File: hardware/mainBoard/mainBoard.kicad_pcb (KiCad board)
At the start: 2 copper layers, 99.9 x 52.5 mm, 24 parts, among them J1 UARTDebug, J2 LeftKeyConnector, J3 DisplayConnector, J4 RightKeyConnector, J5 EncoderConnector, U1 MCP4728-E_UN

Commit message: update wiring
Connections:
- A1 pad 16: Net-(A1-GPIO12) -> unconnected-(A1-GPIO12-Pad16)_1
- A1 pad 17: /LDAC -> unconnected-(A1-GPIO13-Pad17)
- A1 pad 19: unconnected-(A1-GPIO14-Pad19)_1 -> Net-(A1-GPIO14)
- A1 pad 20: unconnected-(A1-GPIO15-Pad20) -> /LDAC
- J3 pad 7: Net-(A1-GPIO12) -> Net-(A1-GPIO14)
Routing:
- net Net-(A1-GPIO12): track 20.3 -> 0.00 mm
- net Net-(A1-GPIO14): track 0.00 -> 13.8 mm
- net (no net): track 0.00 -> 0.80 mm
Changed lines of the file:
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@@
 			(layers "F.Cu" "F.Mask")
 			(roundrect_rratio 0.5)
-			(net "Net-(A1-GPIO12)")
+			(net "unconnected-(A1-GPIO12-Pad16)")
 			(pinfunction "GPIO12_16")
-			(pintype "bidirectional")
+			(pintype "bidirectional+no_connect")
 		)
 		(pad "16" thru_hole circle
@@
 			(layers "*.Cu" "*.Mask")
 			(remove_unused_layers no)
-			(net "Net-(A1-GPIO12)")
+			(net "unconnected-(A1-GPIO12-Pad16)_1")
 			(pinfunction "GPIO12_16")
-			(pintype "bidirectional")
+			(pintype "bidirectional+no_connect")
 		)
 		(pad "17" smd roundrect
@@
 			(layers "F.Cu" "F.Mask")
 			(roundrect_rratio 0.5)
-			(net "/LDAC")
+			(net "unconnected-(A1-GPIO13-Pad17)_1")
 			(pinfunction "GPIO13_17")
-			(pintype "bidirectional")
+			(pintype "bidirectional+no_connect")
 		)
 		(pad "17" thru_hole circle
@@
 			(layers "*.Cu" "*.Mask")
 			(remove_unused_layers no)
-			(net "/LDAC")
+			(net "unconnected-(A1-GPIO13-Pad17)")
 			(pinfunction "GPIO13_17")
-			(pintype "bidirectional")
+			(pintype "bidirectional+no_connect")
 		)
 		(pad "18" smd custom
@@
 			(layers "F.Cu" "F.Mask")
 			(roundrect_rratio 0.5)
-			(net "unconnected-(A1-GPIO14-Pad19)")
+			(net "Net-(A1-GPIO14)")
 			(pinfunction "GPIO14_19")
-			(pintype "bidirectional+no_connect")
+			(pintype "bidirectional")
 		)
 		(pad "19" thru_hole circle
@@
 			(layers "*.Cu" "*.Mask")
 			(remove_unused_layers no)
-			(net "unconnected-(A1-GPIO14-Pad19)_1")
+			(net "Net-(A1-GPIO14)")
 			(pinfunction "GPIO14_19")
-			(pintype "bidirectional+no_connect")
+			(pintype "bidirectional")
 		)
 		(pad "20" smd roundrect
@@
 			(layers "F.Cu" "F.Mask")
 			(roundrect_rratio 0.5)
-			(net "unconnected-(A1-GPIO15-Pad20)_1")
+			(net "/LDAC")
 			(pinfunction "GPIO15_20")
-			(pintype "bidirectional+no_connect")
+			(pintype "bidirectional")
 		)
 		(pad "20" thru_hole circle
@@
 			(layers "*.Cu" "*.Mask")
 			(remove_unused_layers no)
-			(net "unconnected-(A1-GPIO15-Pad20)")
+			(net "/LDAC")
 			(pinfunction "GPIO15_20")
-			(pintype "bidirectional+no_connect")
+			(pintype "bidirectional")
 		)
 		(pad "21" thru_hole circle
@@
 	)
 	(footprint "Connector_PinHeader_2.54mm:PinHeader_1x08_P2.54mm_Vertical"
+		(locked yes)
 		(layer "F.Cu")
 		(at 167.62 75.4 -90)
@@
 			(layers "*.Cu" "*.Mask")
 			(remove_unused_layers no)
-			(net "Net-(A1-GPIO12)")
+			(net "Net-(A1-GPIO14)")
 			(pinfunction "Pin_7_7")
 			(pintype "passive")
@@
 	)
 	(gr_text "CS"
+		(locked yes)
 		(at 163.110625 78.995238 90)
 		(layer "F.SilkS")
@@
 		)
 	)
-	(gr_text "GND"
-		(at 165.650625 80.090476 90)
+	(gr_text "VCC"
+		(at 165.650625 79.9 90)
 		(layer "F.SilkS")
 		(effects
@@
 		)
 	)
-	(gr_text "VCC"
-		(at 168.190625 79.9 90)
+	(gr_text "GND"
+		(at 168.190625 80.090476 90)
 		(layer "F.SilkS")
 		(effects
@@
 	)
 	(segment
+		(start 167.4925 85.31)
+		(end 167.4925 86.11)
+		(width 0.2)
+		(layer "F.Cu")
+		(net "")
+	)
+	(segment
 		(start 147.65 95.5)
 		(end 148.35 96.2)
@@
 	)
 	(segment
-		(start 169.4125 82.95)
-		(end 165.01 82.95)
+		(start 164.51 82.45)
+		(end 157.46 75.4)
 		(width 0.2)
 		(layer "B.Cu")
@@
 	)
 	(segment
-		(start 172.5725 86.11)
-		(end 169.4125 82.95)
+		(start 168.9125 82.45)
+		(end 164.51 82.45)
 		(width 0.2)
 		(layer "B.Cu")
@@
 	)
 	(segment
-		(start 165.01 82.95)
-		(end 157.46 75.4)
+		(start 172.5725 86.11)
+		(end 168.9125 82.45)
 		(width 0.2)
 		(layer "B.Cu")
@@
 	)
 	(segment
-		(start 167.9225 84)
-		(end 163.52 84)
-		(width 0.2)
-		(layer "B.Cu")
-		(net "Net-(A1-GPIO11)")
-	)
-	(segment
 		(start 170.0325 86.11)
-		(end 167.9225 84)
+		(end 167.4225 83.5)
 		(width 0.2)
 		(layer "B.Cu")
@@
 	)
 	(segment
-		(start 154.92 75.4)
-		(end 161.45 81.93)
+		(start 167.4225 83.5)
+		(end 163.02 83.5)
 		(width 0.2)
 		(layer "B.Cu")
@@
 	)
 	(segment
-		(start 163.52 84)
-		(end 161.45 81.93)
+		(start 163.02 83.5)
+		(end 154.92 75.4)
 		(width 0.2)
 		(layer "B.Cu")
@@
 	)
 	(segment
-		(start 167.4925 85.31)
-		(end 167.4925 86.11)
-		(width 0.2)
-		(layer "F.Cu")
-		(net "Net-(A1-GPIO12)")
-	)
-	(segment
-		(start 167.4925 86.11)
-		(end 166.3875 85.005)
-		(width 0.2)
-		(layer "B.Cu")
-		(net "Net-(A1-GPIO12)")
-	)
-	(segment
-		(start 161.985 85.005)
-		(end 152.38 75.4)
-		(width 0.2)
-		(layer "B.Cu")
-		(net "Net-(A1-GPIO12)")
-	)
-	(segment
-		(start 166.3875 85.005)
-		(end 161.985 85.005)
-		(width 0.2)
-		(layer "B.Cu")
-		(net "Net-(A1-GPIO12)")
-	)
-	(segment
 		(start 157.3325 112.0825)
 		(end 157.3325 103.89)
@@
 		(net "Net-(MES4-+)")
 	)
+	(segment
+		(start 159.8725 82.8925)
+		(end 159.8725 86.11)
+		(width 0.2)
+		(layer "B.Cu")
+		(net "Net-(A1-GPIO14)")
+	)
+	(segment
+		(start 152.38 75.4)
+		(end 159.8725 82.8925)
+		(width 0.2)
+		(layer "B.Cu")
+		(net "Net-(A1-GPIO14)")
+	)
 	(zone

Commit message: update wrong ldac pin
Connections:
- A1 pad 17: unconnected-(A1-GPIO13-Pad17) -> /LDAC
- A1 pad 20: /LDAC -> unconnected-(A1-GPIO15-Pad20)
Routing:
- net (no net): track 0.80 -> 0.00 mm
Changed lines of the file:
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@@
 			(layers "F.Cu" "F.Mask")
 			(roundrect_rratio 0.5)
-			(net "unconnected-(A1-GPIO13-Pad17)_1")
+			(net "/LDAC")
 			(pinfunction "GPIO13_17")
-			(pintype "bidirectional+no_connect")
+			(pintype "bidirectional")
 		)
 		(pad "17" thru_hole circle
@@
 			(layers "*.Cu" "*.Mask")
 			(remove_unused_layers no)
-			(net "unconnected-(A1-GPIO13-Pad17)")
+			(net "/LDAC")
 			(pinfunction "GPIO13_17")
-			(pintype "bidirectional+no_connect")
+			(pintype "bidirectional")
 		)
 		(pad "18" smd custom
@@
 			(layers "F.Cu" "F.Mask")
 			(roundrect_rratio 0.5)
-			(net "/LDAC")
+			(net "unconnected-(A1-GPIO15-Pad20)")
 			(pinfunction "GPIO15_20")
 			(pintype "bidirectional")
@@
 			(layers "*.Cu" "*.Mask")
 			(remove_unused_layers no)
-			(net "/LDAC")
+			(net "unconnected-(A1-GPIO15-Pad20)")
 			(pinfunction "GPIO15_20")
 			(pintype "bidirectional")
@@
 	)
 	(segment
-		(start 167.4925 85.31)
-		(end 167.4925 86.11)
-		(width 0.2)
-		(layer "F.Cu")
-		(net "")
-	)
-	(segment
 		(start 147.65 95.5)
 		(end 148.35 96.2)
@@
 	)
 	(segment
+		(start 159.8725 82.8925)
+		(end 159.8725 86.11)
+		(width 0.2)
+		(layer "B.Cu")
+		(net "Net-(A1-GPIO14)")
+	)
+	(segment
+		(start 152.38 75.4)
+		(end 159.8725 82.8925)
+		(width 0.2)
+		(layer "B.Cu")
+		(net "Net-(A1-GPIO14)")
+	)
+	(segment
 		(start 157.3325 112.0825)
 		(end 157.3325 103.89)
@@
 		(net "Net-(MES4-+)")
 	)
-	(segment
-		(start 159.8725 82.8925)
-		(end 159.8725 86.11)
-		(width 0.2)
-		(layer "B.Cu")
-		(net "Net-(A1-GPIO14)")
-	)
-	(segment
-		(start 152.38 75.4)
-		(end 159.8725 82.8925)
-		(width 0.2)
-		(layer "B.Cu")
-		(net "Net-(A1-GPIO14)")
-	)
 	(zone

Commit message: add led headers to main board
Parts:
- removed the J5 at (179.2, 113.9)
- added J4: LEDHeader, Connector_JST:JST_XH_B3B-XH-A_1x03_P2.50mm_Vertical, F.Cu at (151.0, 102.9)
- added J6: EncoderConnector, Connector_JST:JST_XH_B5B-XH-A_1x05_P2.50mm_Vertical, F.Cu at (178.7, 114.0)
- renumbered J4 to J5
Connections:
- A1 pad 20: unconnected-(A1-GPIO15-Pad20) -> Net-(A1-GPIO15)
- A1 pad 31: unconnected-(A1-GPIO26_ADC0-Pad31)_1 -> Net-(A1-GPIO26_ADC0)
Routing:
- net +5V: track 0.73 -> 58.3 mm
- net Net-(A1-GPIO15): track 0.00 -> 22.7 mm
- net Net-(A1-GPIO26_ADC0): track 0.00 -> 11.5 mm
- net +3V3: track 141.5 -> 149.0 mm

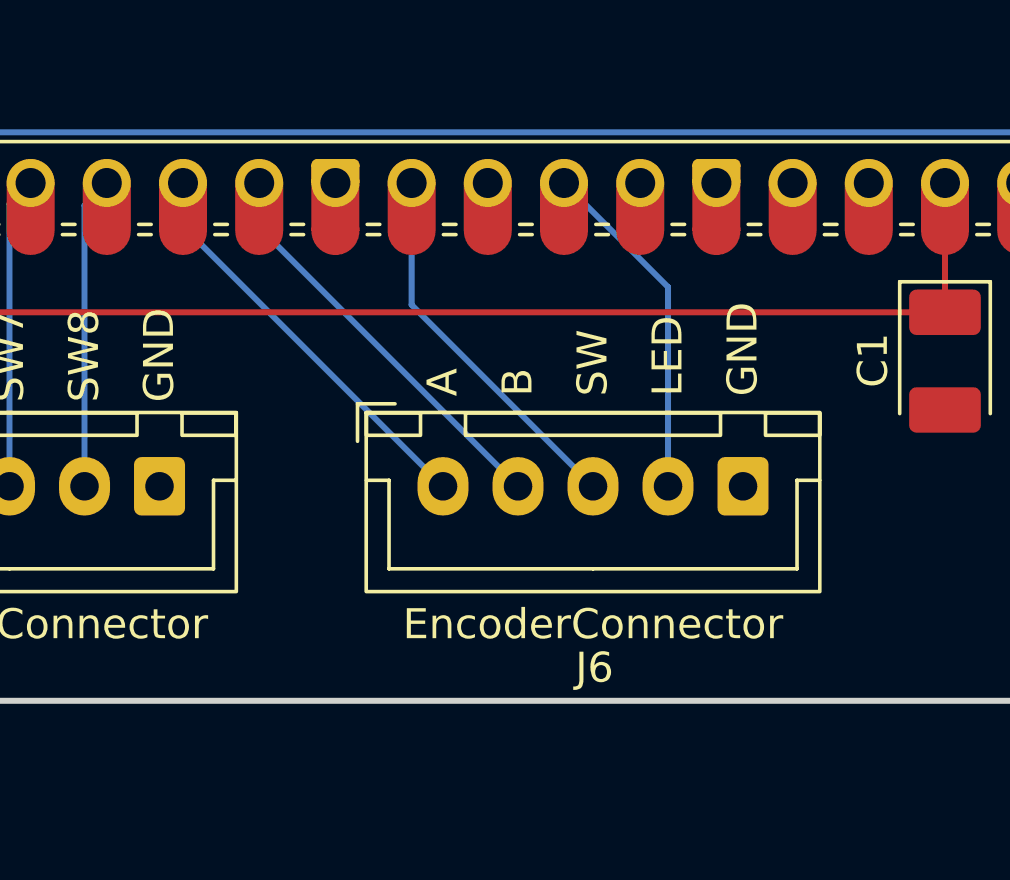
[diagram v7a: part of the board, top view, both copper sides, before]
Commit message: add led header to pcb
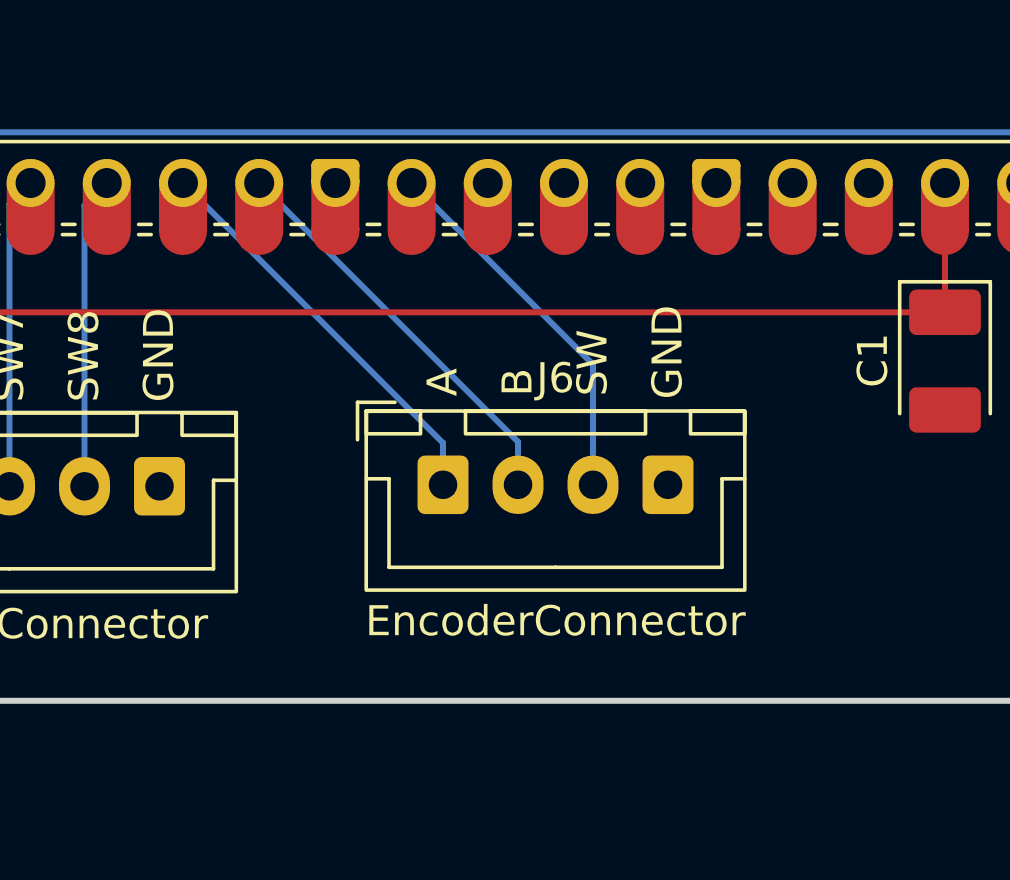
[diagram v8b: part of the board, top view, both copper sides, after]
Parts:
- J6: footprint Connector_JST:JST_XH_B5B-XH-A_1x05_P2.50mm_Vertical -> Connector_JST:JST_XH_B4B-XH-A_1x04_P2.50mm_Vertical
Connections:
- A1 pad 31: Net-(A1-GPIO26_ADC0) -> unconnected-(A1-GPIO26_ADC0-Pad31)
- J6 pad 4: Net-(A1-GPIO26_ADC0) -> GND
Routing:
- net Net-(A1-GPIO26_ADC0): track 11.5 -> 0.00 mm
